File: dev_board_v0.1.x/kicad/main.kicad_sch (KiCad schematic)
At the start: 1 part, among them U1 RP2040

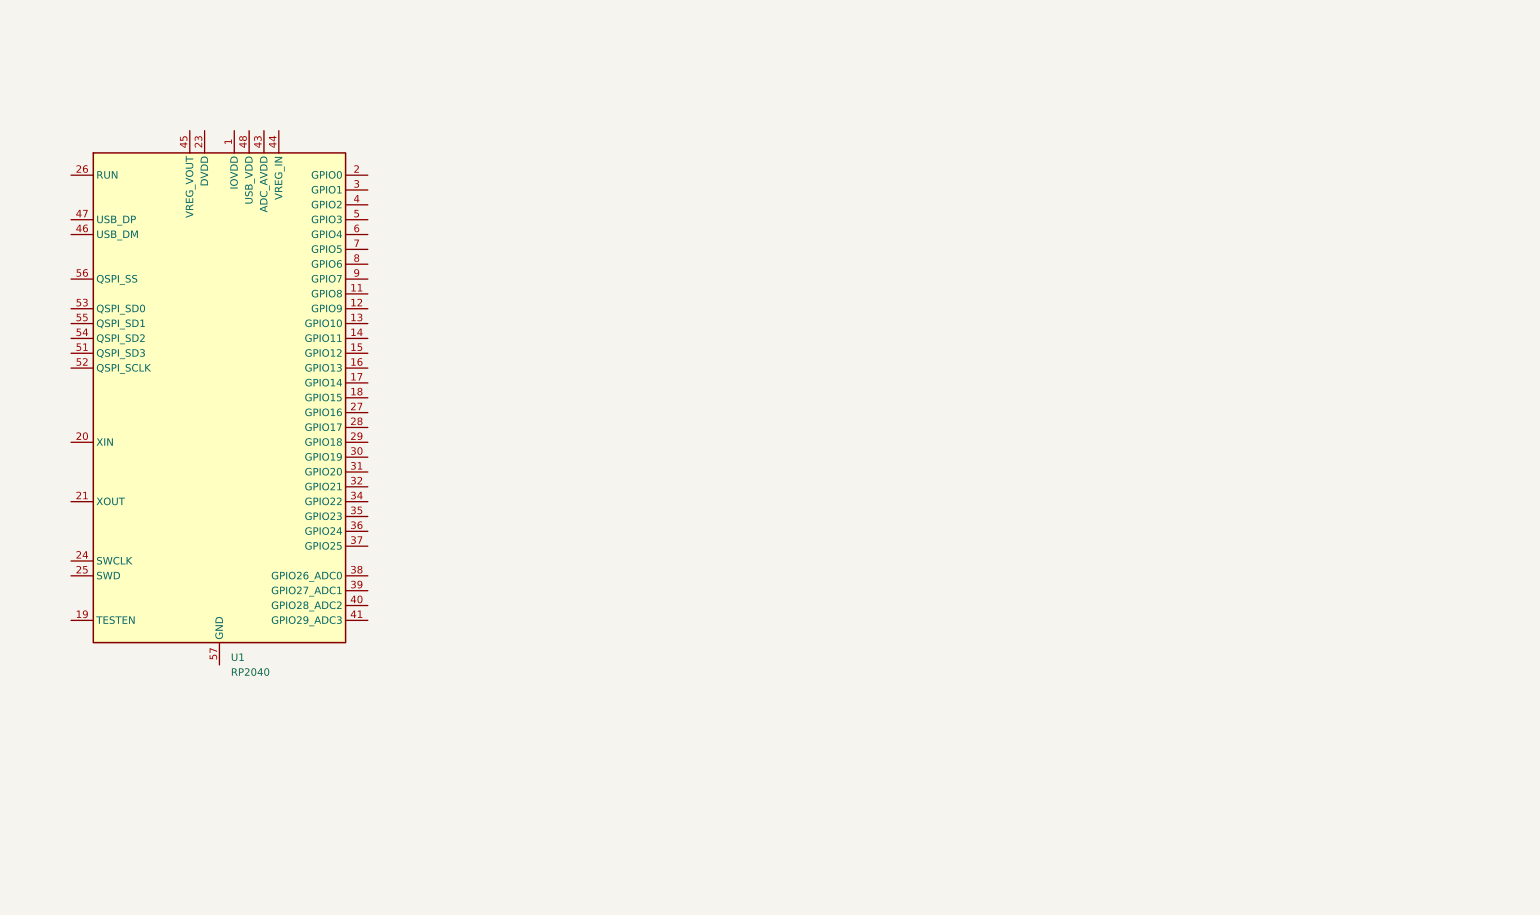
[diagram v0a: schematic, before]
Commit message: feat: add power net
add decoupling capacitor to MCU
build 1v1 and 3v3 power bus
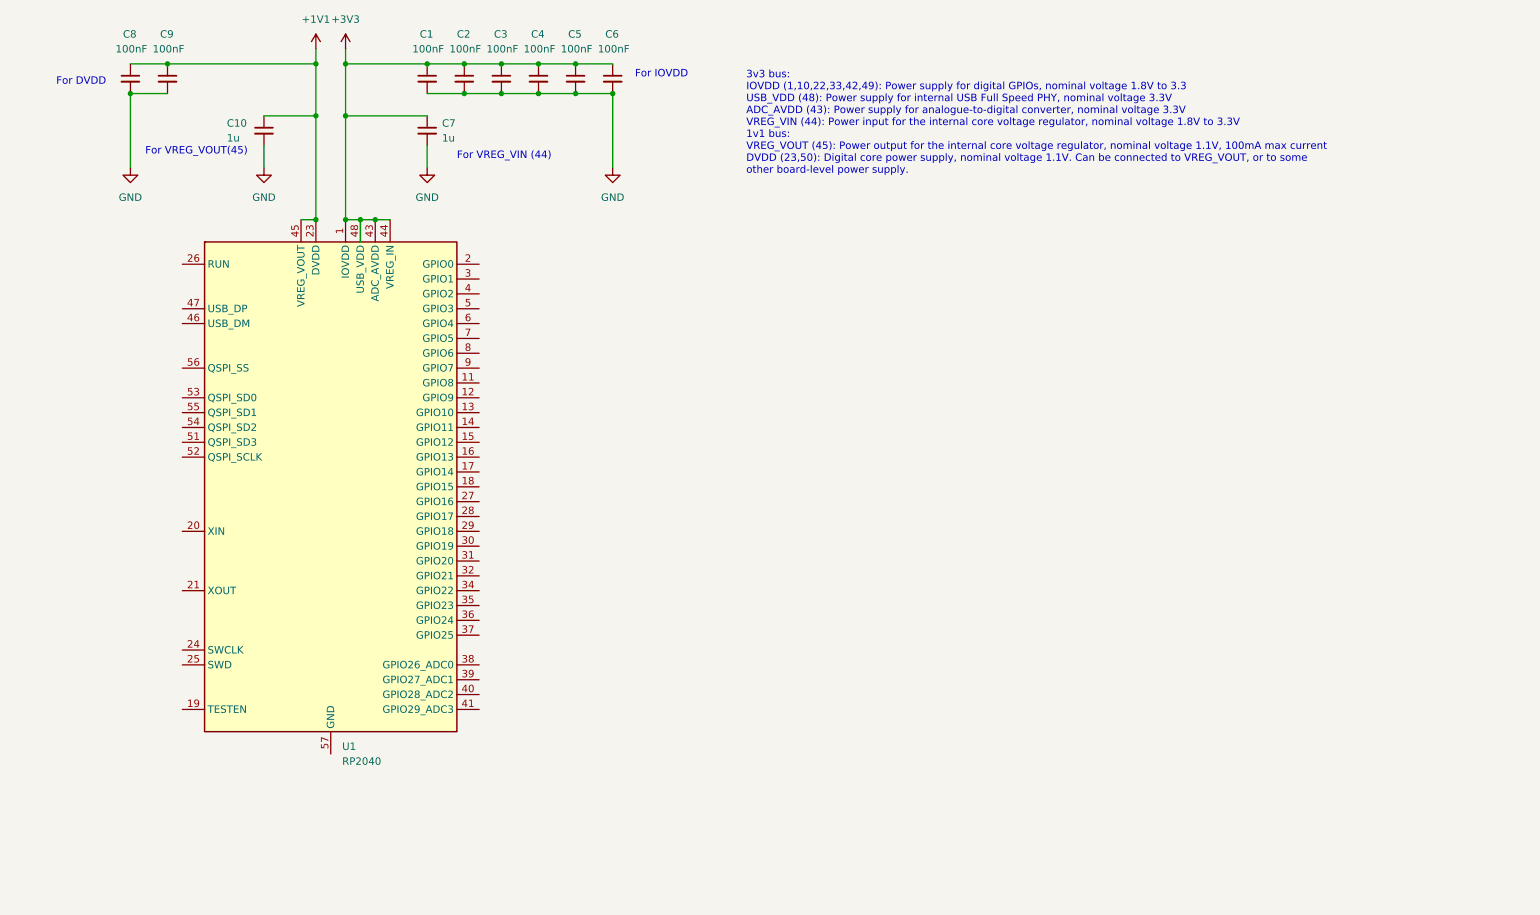
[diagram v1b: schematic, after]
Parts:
- added C1, C2, C3, C4, C5, C6, C8, C9: 100nF, Resistor_SMD:R_0603_1608Metric, symbol Device:C_Small
- added C10, C7: 1u, Resistor_SMD:R_0603_1608Metric, symbol Device:C_Small
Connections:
- net +3V3: now reaches U1.1 (IOVDD), U1.10 (IOVDD), U1.22 (IOVDD), U1.33 (IOVDD), U1.42 (IOVDD), U1.49 (IOVDD)
- net +3V3: now also U1.43 (ADC_AVDD), U1.44 (VREG_IN), U1.48 (USB_VDD), C1.1, C2.1, C3.1, C4.1, C5.1, C6.1, C7.1
- net +1V1: now reaches U1.23 (DVDD), U1.50 (DVDD)
- net +1V1: now also U1.45 (VREG_VOUT), C10.1, C8.1, C9.1
- new net GND: C1.2, C10.2, C2.2, C3.2, C4.2, C5.2, C6.2, C7.2, C8.2, C9.2
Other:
- note added: "3v3 bus: IOVDD (1,10,22,33,42,49): Power supply for digital GPIOs, nominal voltage 1.8V to 3.3 USB_VDD (48): Power supply for internal USB Full Speed PHY, nominal voltage 3.3V ADC_AVDD (43): Power supply for analogue-to-digital converter, nominal voltage 3.3V VREG_VIN (44): Power input for the internal core voltage regulator, nominal voltage 1.8V to 3.3V 1v1 bus: VREG_VOUT (45): Power output for 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"
- note added: "For DVDD"
- note added: "For IOVDD"
- note added: "For VREG_VIN (44)"
- note added: "For VREG_VOUT(45)"
- company: (none) -> Micro Henry
- title: (none) -> RP2040 Dev Board
- moved on the sheet: U1

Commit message: feat: complete mcu basic circuit design
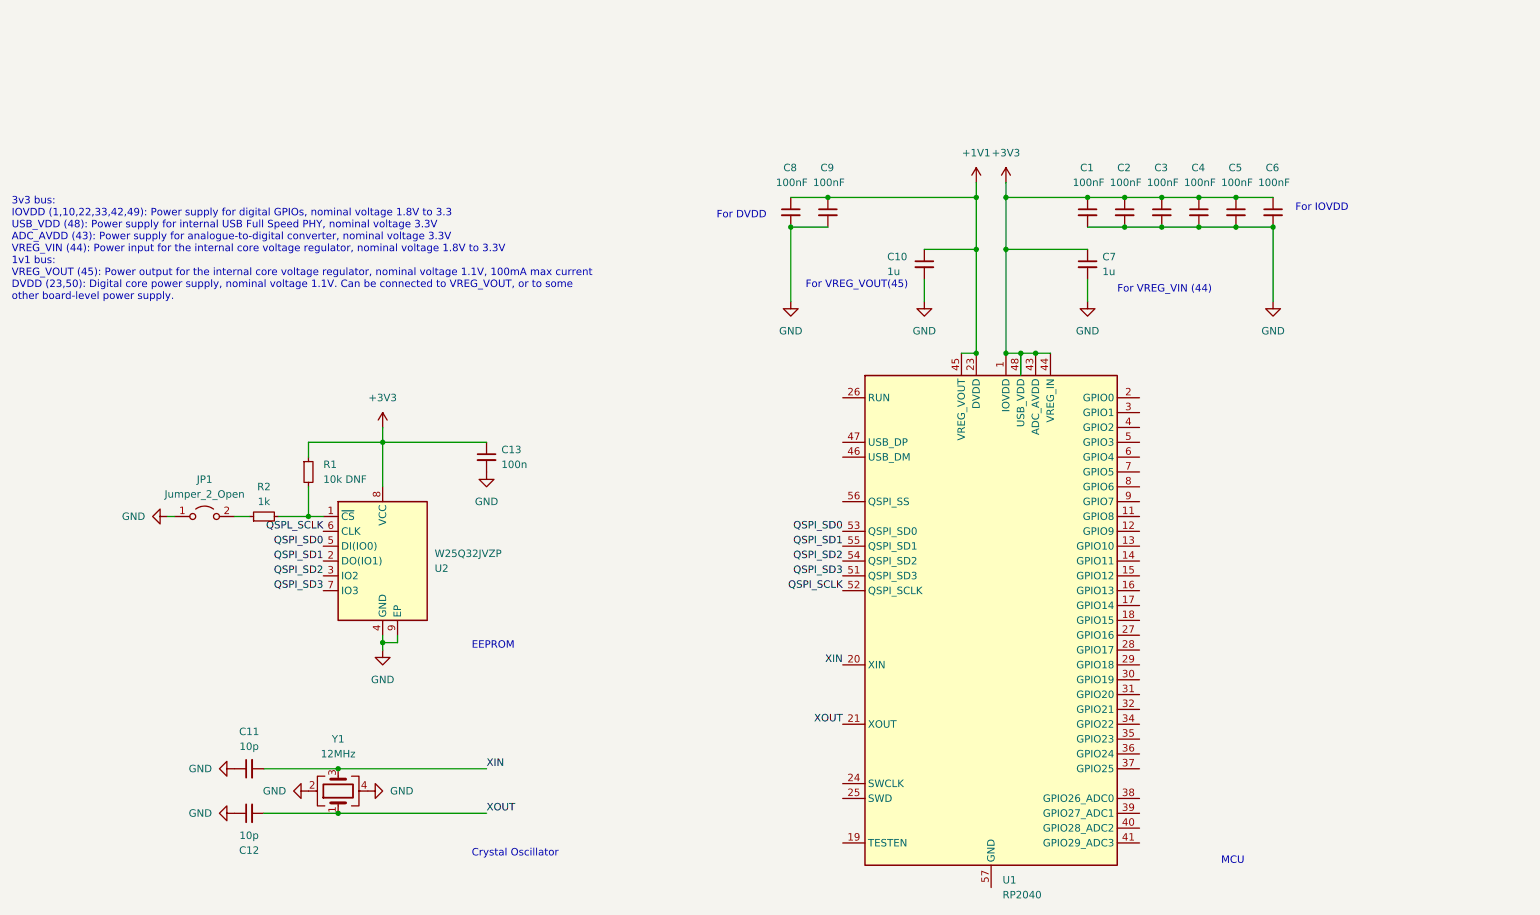
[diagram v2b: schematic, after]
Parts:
- added C11: 10p, Capacitor_SMD:C_0603_1608Metric, symbol Device:C_Small
- added C12: 10p, symbol Device:C_Small
- added C13: 100n, symbol Device:C_Small
- added JP1: Jumper_2_Open, symbol Jumper:Jumper_2_Open
- added R1: 10k DNF, symbol Device:R_Small
- added R2: 1k, symbol Device:R_Small
- added U2: W25Q32JVZP, Package_SON:WSON-8-1EP_6x5mm_P1.27mm_EP3.4x4.3mm, symbol Memory_Flash:W25Q32JVZP
- added Y1: 12MHz, Crystal:Crystal_SMD_3225-4Pin_3.2x2.5mm, symbol Device:Crystal_GND24
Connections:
- net +3V3: now also C13.1, R1.1, U2.8 (VCC)
- net GND: now also C11.1, C12.1, C13.2, JP1.1 (A), U2.4 (GND), U2.9 (EP), Y1.2, Y1.4
- net XIN: now reaches U1.20 (XIN)
- net XIN: now also C11.2, Y1.3
- net XOUT: now reaches U1.21 (XOUT)
- net XOUT: now also C12.2, Y1.1
- net QSPI_SD3: now reaches U1.51 (QSPI_SD3)
- net QSPI_SD3: now also U2.7 (IO3)
- net QSPI_SCLK: now reaches U1.52 (QSPI_SCLK)
- net QSPI_SD0: now reaches U1.53 (QSPI_SD0)
- net QSPI_SD0: now also U2.5 (DI(IO0))
- net QSPI_SD2: now reaches U1.54 (QSPI_SD2)
- net QSPI_SD2: now also U2.3 (IO2)
- net QSPI_SD1: now reaches U1.55 (QSPI_SD1)
- net QSPI_SD1: now also U2.2 (DO(IO1))
- new net: JP1.2 (B), R2.1
- new net: R1.2, R2.2, U2.1 (~{CS})
- new net QSPL_SCLK: U2.6 (CLK)
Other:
- note added: "Crystal Oscillator"
- note added: "EEPROM"
- note added: "MCU"
- moved on the sheet: C1, C10, C2, C3, C4, C5, C6, C7, C8, C9, U1
